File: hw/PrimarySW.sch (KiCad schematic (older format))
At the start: 21 parts

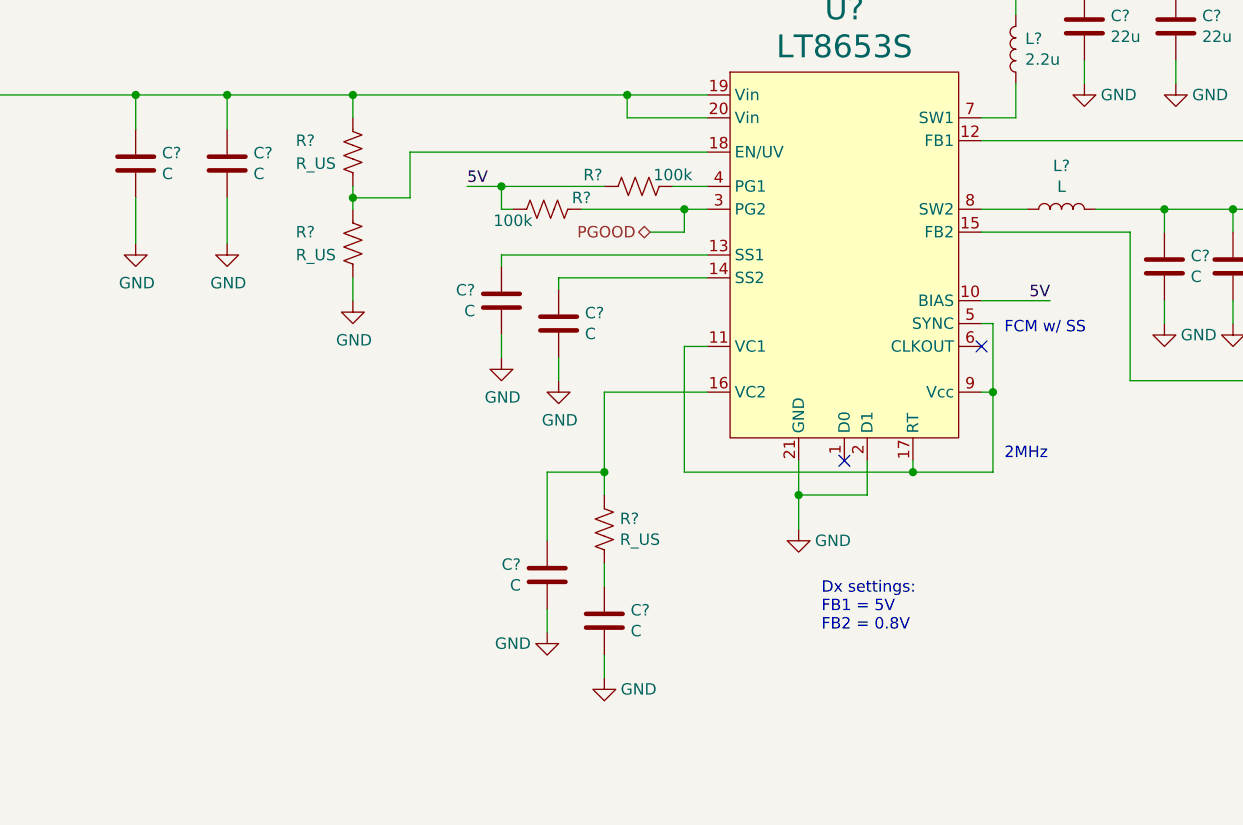
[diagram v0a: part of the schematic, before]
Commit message: Primary SW component selection
selected some components for primary switcher, added AuxOut block, dropped down primary linear reg IC
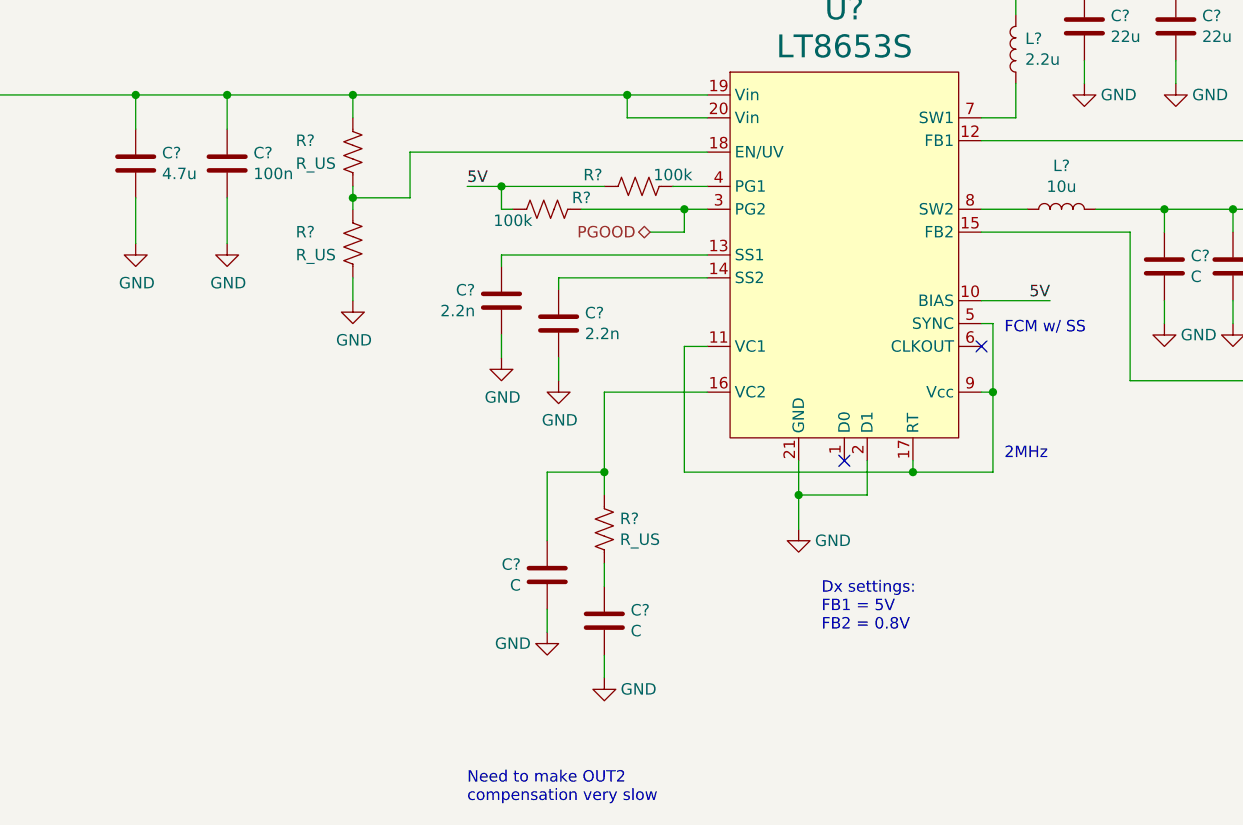
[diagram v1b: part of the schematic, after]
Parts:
- removed C?: C, symbol Device:C
- added C?: 2.2n, Capacitor_SMD:C_0603_1608Metric, symbol Device:C
- C?: value C -> 4.7u; footprint (none) -> Capacitor_SMD:C_1210_3225Metric_Pad1.42x2.65mm_HandSolder
- C?: value C -> 100n; footprint (none) -> Capacitor_SMD:C_0603_1608Metric
- C?: value C -> 2.2n; footprint (none) -> Capacitor_SMD:C_0603_1608Metric
- L?: footprint (none) -> Inductor_SMD:L_Coilcraft_XxL4020
- L?: value L -> 10u; footprint (none) -> Inductor_SMD:L_Coilcraft_XAL5030
- R? (x4): footprint (none) -> Resistor_SMD:R_0603_1608Metric
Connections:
- net GND: now also C?.2
- net at U?.13 (SS1): now also C?.1
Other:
- note added: "Need to make OUT2\ncompensation very slow"
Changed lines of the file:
@@
 $Descr A4 11693 8268
 encoding utf-8
-Sheet 4 6
+Sheet 4 7
 Title ""
 Date ""
@@
 P 2700 2600
 F 0 "C?" H 2815 2646 50  0000 L CNN
-F 1 "C" H 2815 2555 50  0000 L CNN
-F 2 "" H 2738 2450 50  0001 C CNN
+F 1 "4.7u" H 2815 2555 50  0000 L CNN
+F 2 "Capacitor_SMD:C_1210_3225Metric_Pad1.42x2.65mm_HandSolder" H 2738 2450 50  0001 C CNN
 F 3 "~" H 2700 2600 50  0001 C CNN
 	1    2700 2600
@@
 F 0 "L?" H 6509 2146 50  0000 R CNN
 F 1 "2.2u" H 6509 2055 50  0000 R CNN
-F 2 "" H 6550 2100 50  0001 C CNN
+F 2 "Inductor_SMD:L_Coilcraft_XxL4020" H 6550 2100 50  0001 C CNN
 F 3 "~" H 6550 2100 50  0001 C CNN
 F 4 "Coilcraft XFL4020-222ME" H 6550 2100 50  0001 C CNN "MfrNum"
@@
 P 6750 2800
 F 0 "L?" V 6940 2800 50  0000 C CNN
-F 1 "L" V 6849 2800 50  0000 C CNN
-F 2 "" H 6750 2800 50  0001 C CNN
+F 1 "10u" V 6849 2800 50  0000 C CNN
+F 2 "Inductor_SMD:L_Coilcraft_XAL5030" H 6750 2800 50  0001 C CNN
 F 3 "~" H 6750 2800 50  0001 C CNN
 	1    6750 2800
@@
 P 3100 2600
 F 0 "C?" H 3215 2646 50  0000 L CNN
-F 1 "C" H 3215 2555 50  0000 L CNN
-F 2 "" H 3138 2450 50  0001 C CNN
+F 1 "100n" H 3215 2555 50  0000 L CNN
+F 2 "Capacitor_SMD:C_0603_1608Metric" H 3138 2450 50  0001 C CNN
 F 3 "~" H 3100 2600 50  0001 C CNN
 	1    3100 2600
@@
 F 0 "R?" V 4850 2500 50  0000 C CNN
 F 1 "100k" V 4850 2850 50  0000 C CNN
-F 2 "" V 4940 2690 50  0001 C CNN
+F 2 "Resistor_SMD:R_0603_1608Metric" V 4940 2690 50  0001 C CNN
 F 3 "~" H 4900 2700 50  0001 C CNN
 	1    4900 2700
@@
 F 0 "R?" V 4450 2950 50  0000 C CNN
 F 1 "100k" V 4550 2650 50  0000 C CNN
-F 2 "" V 4540 2790 50  0001 C CNN
+F 2 "Resistor_SMD:R_0603_1608Metric" V 4540 2790 50  0001 C CNN
 F 3 "~" H 4500 2800 50  0001 C CNN
 	1    4500 2800
@@
 $Comp
 L Device:C C?
-U 1 1 5E8AEB3A
-P 4300 3200
-F 0 "C?" H 4415 3246 50  0000 L CNN
-F 1 "C" H 4415 3155 50  0000 L CNN
-F 2 "" H 4338 3050 50  0001 C CNN
-F 3 "~" H 4300 3200 50  0001 C CNN
-	1    4300 3200
-	-1   0    0    -1
-$EndComp
-$Comp
-L Device:C C?
 U 1 1 5E8AEC15
 P 4550 3300
 F 0 "C?" H 4665 3346 50  0000 L CNN
-F 1 "C" H 4665 3255 50  0000 L CNN
-F 2 "" H 4588 3150 50  0001 C CNN
+F 1 "2.2n" H 4665 3255 50  0000 L CNN
+F 2 "Capacitor_SMD:C_0603_1608Metric" H 4588 3150 50  0001 C CNN
 F 3 "~" H 4550 3300 50  0001 C CNN
 	1    4550 3300
@@
 F 0 "R?" H 3400 3000 50  0000 L CNN
 F 1 "R_US" H 3400 2900 50  0000 L CNN
-F 2 "" V 3690 2940 50  0001 C CNN
+F 2 "Resistor_SMD:R_0603_1608Metric" V 3690 2940 50  0001 C CNN
 F 3 "~" H 3650 2950 50  0001 C CNN
 	1    3650 2950
@@
 Wire Wire Line
 	3100 2300 3650 2300
-$Comp
-L Device:R_US R?
-U 1 1 5E9023EC
-P 3650 2550
-F 0 "R?" H 3400 2600 50  0000 L CNN
-F 1 "R_US" H 3400 2500 50  0000 L CNN
-F 2 "" V 3690 2540 50  0001 C CNN
-F 3 "~" H 3650 2550 50  0001 C CNN
-	1    3650 2550
-	1    0    0    -1
-$EndComp
 Wire Wire Line
 	3650 2400 3650 2300
@@
 Wire Wire Line
 	8450 3300 8100 3300
+$Comp
+L Device:R_US R?
+U 1 1 5E9023EC
+P 3650 2550
+F 0 "R?" H 3400 2600 50  0000 L CNN
+F 1 "R_US" H 3400 2500 50  0000 L CNN
+F 2 "Resistor_SMD:R_0603_1608Metric" V 3690 2540 50  0001 C CNN
+F 3 "~" H 3650 2550 50  0001 C CNN
+	1    3650 2550
+	1    0    0    -1
+$EndComp
+$Comp
+L Device:C C?
+U 1 1 5EB74DC5
+P 4300 3200
+F 0 "C?" H 4415 3246 50  0000 L CNN
+F 1 "2.2n" H 4415 3155 50  0000 L CNN
+F 2 "Capacitor_SMD:C_0603_1608Metric" H 4338 3050 50  0001 C CNN
+F 3 "~" H 4300 3200 50  0001 C CNN
+	1    4300 3200
+	-1   0    0    -1
+$EndComp
+Text Notes 4150 5400 0    50   ~ 0
+Need to make OUT2\ncompensation very slow
 $EndSCHEMATC

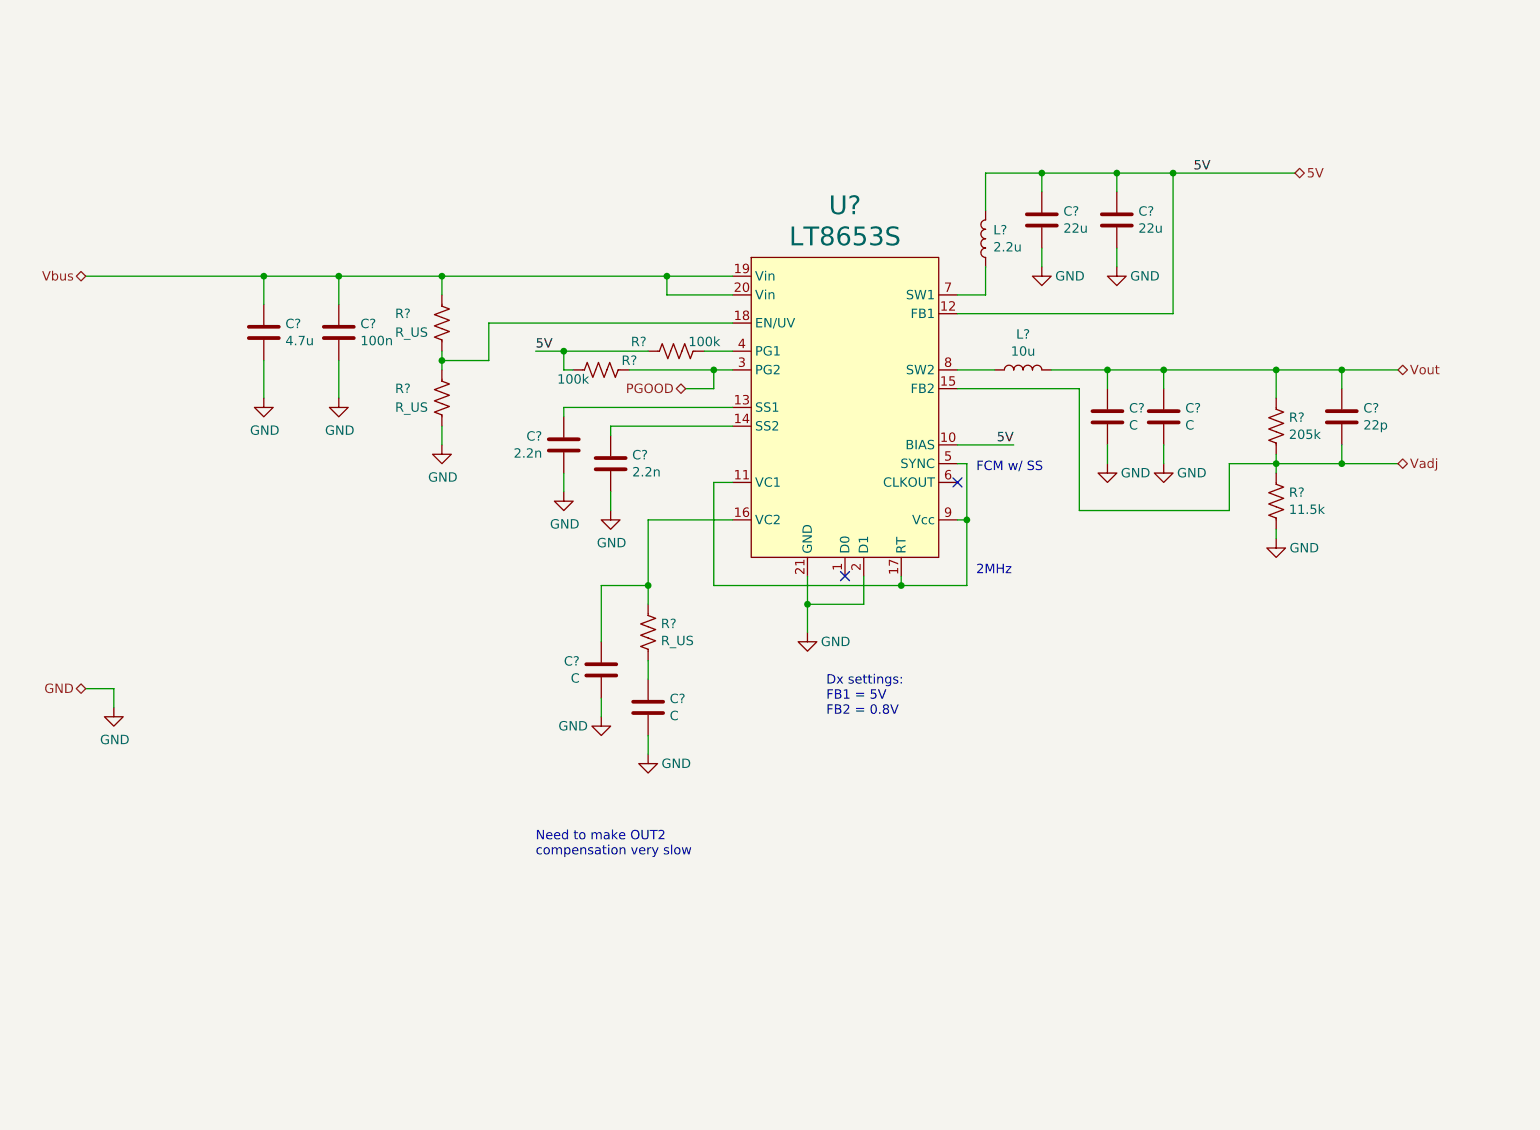
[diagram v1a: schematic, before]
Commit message: Cap selections
Lots of capacitor selections & datasheet downloads

Updated LTPowerCAD model with initial compensation values for primary switcher
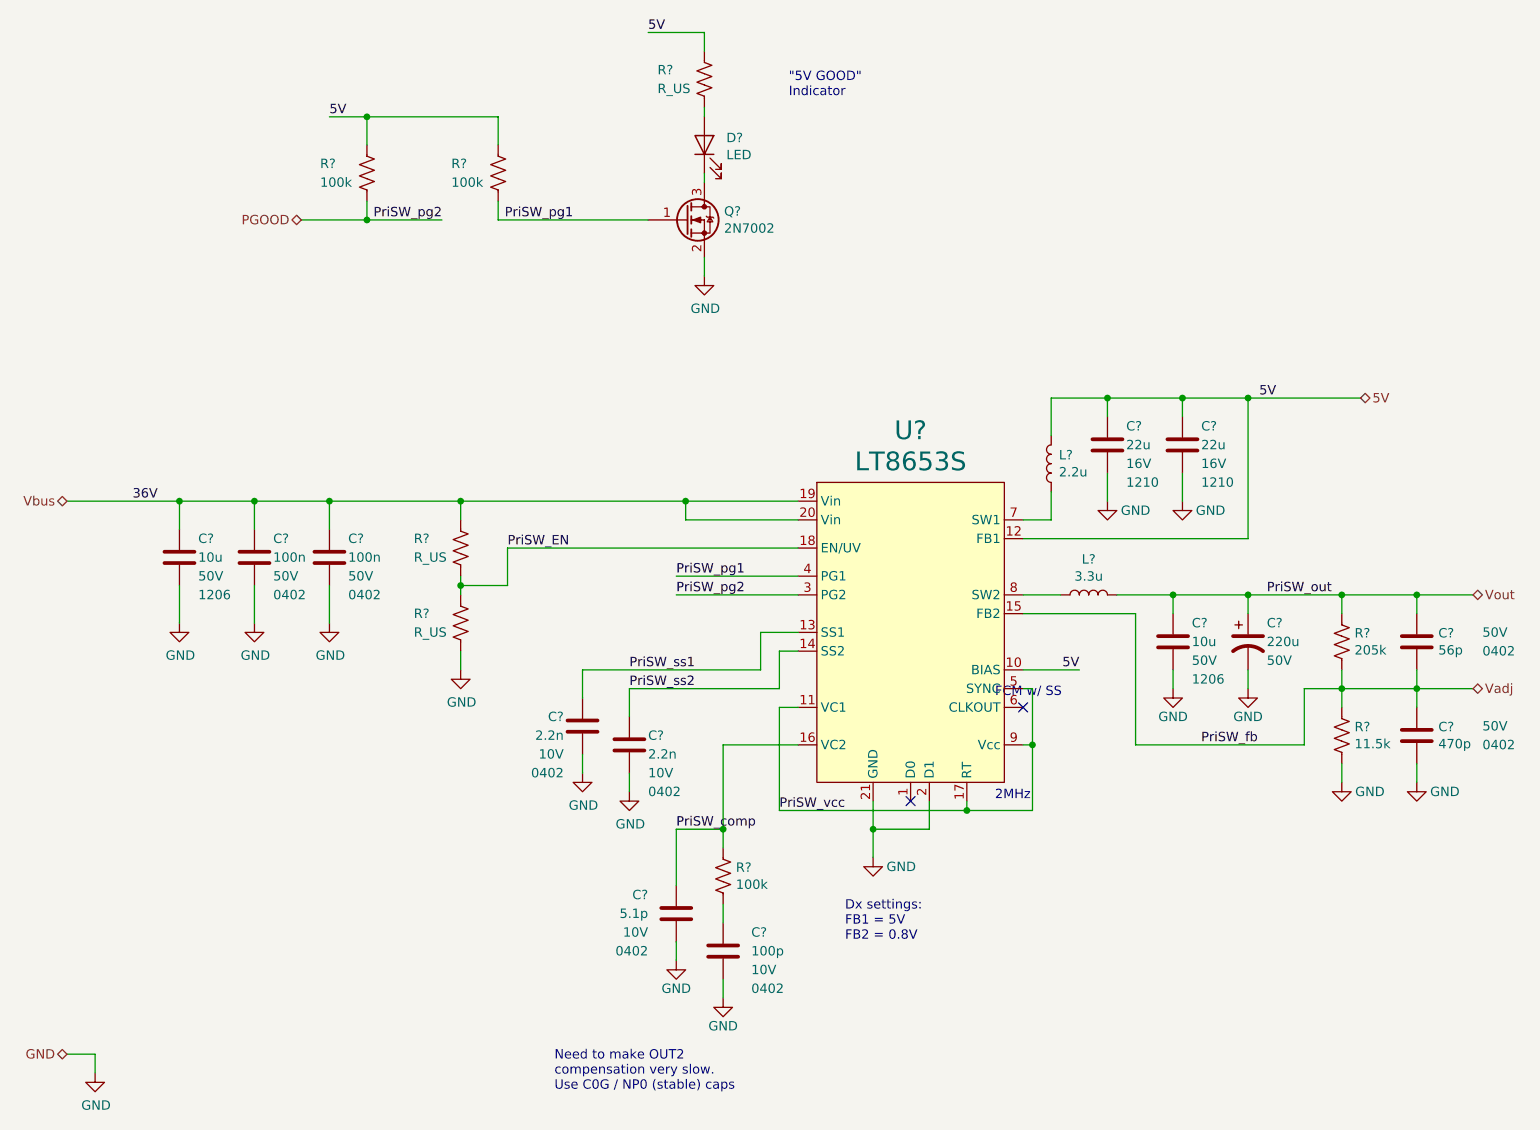
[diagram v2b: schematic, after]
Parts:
- removed C?: 4.7u, Capacitor_SMD:C_1210_3225Metric_Pad1.42x2.65mm_HandSolder, symbol Device:C
- removed C?: 22u, symbol Device:C
- removed C? (x2): C, symbol Device:C
- removed C?: 2.2n, Capacitor_SMD:C_0603_1608Metric, symbol Device:C
- removed R? (x2): 100k, Resistor_SMD:R_0603_1608Metric, symbol Device:R_US
- added C?: 470p, Resistor_SMD:R_0603_1608Metric, symbol Device:C
- added C?: 22u, symbol Device:C
- added C?: 10u, Capacitor_SMD:C_1206_3216Metric_Pad1.42x1.75mm_HandSolder, symbol Device:C
- added C?: 220u, symbol Device:CP1
- added C?: 100n, Capacitor_SMD:C_0603_1608Metric, symbol Device:C
- added C?: 2.2n, Capacitor_SMD:C_0603_1608Metric, symbol Device:C
- added C?: 5.1p, Capacitor_SMD:C_0603_1608Metric, symbol Device:C
- added D?: LED, LED_SMD:LED_0603_1608Metric, symbol Device:LED
- added Q?: 2N7002, Package_TO_SOT_SMD:SOT-323_SC-70, symbol Device:Q_NMOS_GSD
- added R? (x2): 100k, Resistor_SMD:R_0603_1608Metric, symbol Device:R_US
- added R?: R_US, Resistor_SMD:R_0603_1608Metric, symbol Device:R_US
- C?: MfrNum (none) -> TDK_C3225X5R1C226K250AA; Size (none) -> 1210; VRating (none) -> 16V
- C?: value C -> 10u; MfrNum (none) -> Murata_GRT31CR61H106ME01; Size (none) -> 1206; VRating (none) -> 50V
- C?: MfrNum (none) -> Murata_GRM155R61H104KE19D; Size (none) -> 0402; VRating (none) -> 50V
- C?: Size (none) -> 0402; VRating (none) -> 10V
- C?: value C -> 100p; footprint (none) -> Capacitor_SMD:C_0603_1608Metric; Size (none) -> 0402; VRating (none) -> 10V
- C?: value 22p -> 56p; footprint (none) -> Resistor_SMD:R_0603_1608Metric; MfrNum (none) -> findapart; Size (none) -> 0402; VRating (none) -> 50V
- L?: MfrNum Coilcraft XFL4020-222ME -> Coilcraft_XFL4020-222ME
- L?: value 10u -> 3.3u; MfrNum (none) -> Coilcraft_XAL5030-332ME
- R?: value R_US -> 100k; footprint (none) -> Resistor_SMD:R_0603_1608Metric
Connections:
- net 5V: now also C?.1, R?.1, R?.1, R?.1
- net GND: now also C?.2, C?.2, C?.2, C?.2, C?.2, C?.2, C?.2, Q?.2 (S)
- net PGOOD: now also R?.2
- net Vadj: now also C?.1
- net Vbus: now also C?.1, C?.1
- net Vout: now also C?.1
- net PriSW_vcc: now reaches U?.11 (VC1), U?.17 (RT), U?.5 (SYNC), U?.9 (Vcc)
- net PriSW_ss1: now reaches U?.13 (SS1)
- net PriSW_ss1: now also C?.1
- net PriSW_ss2: now reaches C?.1, U?.14 (SS2)
- net PriSW_comp: now reaches R?.1, U?.16 (VC2)
- net PriSW_comp: now also C?.1
- net PriSW_EN: now reaches R?.1, R?.2, U?.18 (EN/UV)
- net PriSW_pg1: now reaches U?.4 (PG1)
- net PriSW_pg1: now also Q?.1 (G), R?.2
- new net: D?.1 (K), Q?.3 (D)
- new net: D?.2 (A), R?.2
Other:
- note added: ""5V GOOD"\nIndicator"
- note added: "Need to make OUT2\ncompensation very slow.\nUse C0G / NP0 (stable) caps"
- note removed: "Need to make OUT2\ncompensation very slow"
- moved on the sheet: C?, L?, R?, U?

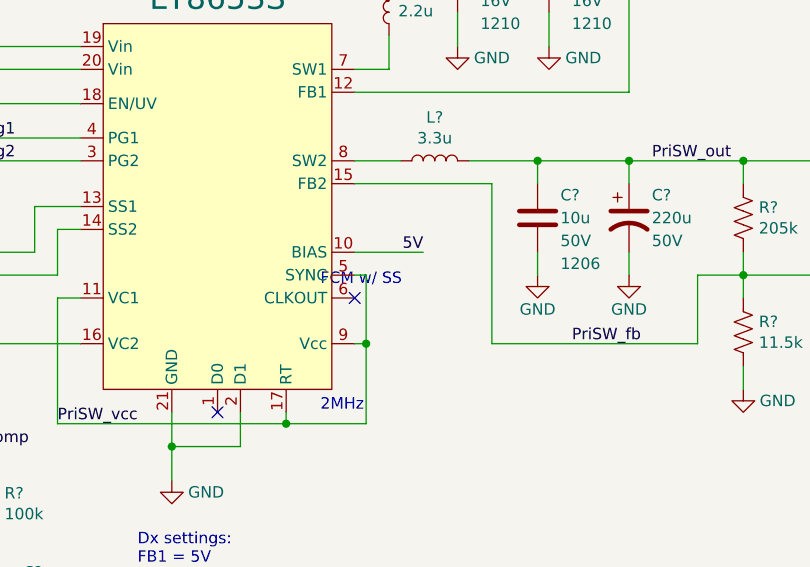
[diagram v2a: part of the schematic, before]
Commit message: more component selection
more caps selected; updated primary switcher sim file
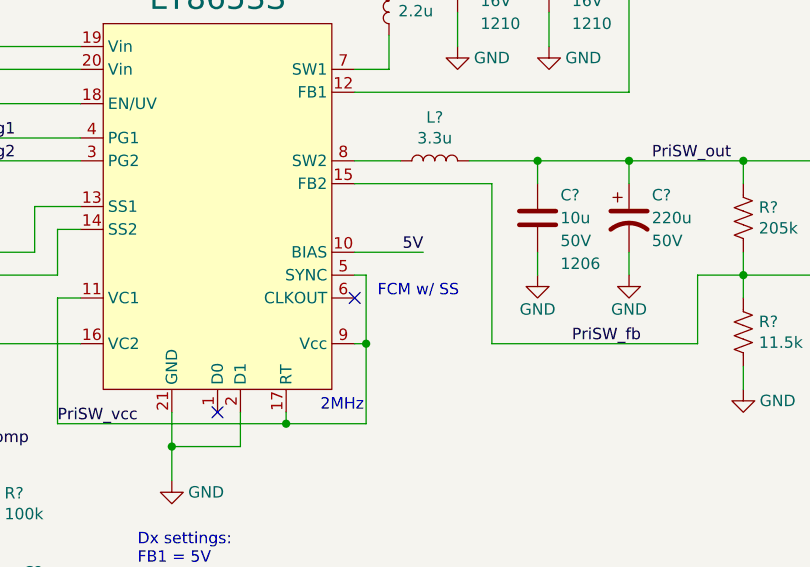
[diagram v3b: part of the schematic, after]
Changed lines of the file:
@@
 Wire Wire Line
 	6800 4500 6750 4500
-Text Notes 6600 4550 0    50   ~ 0
+Text Notes 6850 4600 0    50   ~ 0
 FCM w/ SS
 $Comp
@@
 	1    0    0    -1
 $EndComp
-$Comp
-L Device:R_US R?
-U 1 1 5EC4E1C3
-P 3950 1750
-F 0 "R?" H 3700 1800 50  0000 L CNN
-F 1 "100k" H 3700 1700 50  0000 L CNN
-F 2 "Resistor_SMD:R_0603_1608Metric" V 3990 1740 50  0001 C CNN
-F 3 "~" H 3950 1750 50  0001 C CNN
-	1    3950 1750
-	1    0    0    -1
-$EndComp
 Wire Wire Line
 	5550 4000 4900 4000
@@
 Wire Wire Line
 	8450 5000 8450 4900
+$Comp
+L Device:R_US R?
+U 1 1 5EC4E1C3
+P 3950 1750
+F 0 "R?" H 3700 1800 50  0000 L CNN
+F 1 "100k" H 3700 1700 50  0000 L CNN
+F 2 "Resistor_SMD:R_0603_1608Metric" V 3990 1740 50  0001 C CNN
+F 3 "~" H 3950 1750 50  0001 C CNN
+	1    3950 1750
+	1    0    0    -1
+$EndComp
 $EndSCHEMATC
